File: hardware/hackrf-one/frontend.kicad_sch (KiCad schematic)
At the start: 143 parts

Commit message: HackRF One: update trace widths for new stack-up
correct or ignore ERC/DRC errors
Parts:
- C1, C11, C24, C29, C3, C33, C34, C35, C36, C37, C38, C39, C40, C45, C47, C5, C55, C57, C60, C63, C65, C66, C67, C7: value (none) -> 33pF; footprint (none) -> hackrf:GSG-0402
- C10, C16, C162, C163, C19, C2, C22, C30, C4, C54, C56, C6: value (none) -> 10nF; footprint (none) -> hackrf:GSG-0402
- C12, C13: value (none) -> 330pF; footprint (none) -> hackrf:GSG-0402
- C14: value (none) -> 8p2; footprint (none) -> hackrf:GSG-0402
- C15: value (none) -> 180pF; footprint (none) -> hackrf:GSG-0402
- C160, C41, C42, C52, C70: value (none) -> 100pF; footprint (none) -> hackrf:GSG-0402
- C161, C171, C53: value (none) -> 1uF; footprint (none) -> hackrf:GSG-0402
- C166, C17, C18, C20, C23, C25, C28, C31, C44, C46, C49, C50, C58, C59, C61, C62, C64, C9: value (none) -> 100nF; footprint (none) -> hackrf:GSG-0402
- C21, C32, C43, C48, C51, C8: value (none) -> 22pF; footprint (none) -> hackrf:GSG-0402
- C26, C27: value (none) -> 47pF; footprint (none) -> hackrf:GSG-0402
- D1: value (none) -> GSG-DIODE-TVS-BI; footprint (none) -> hackrf:GSG-0402
- J10: value (none) -> GND_CLIP; footprint (none) -> hackrf:GSG-TEST-POINT-S1751-46R
- J2: value (none) -> RF-SHIELD-FRAME; footprint (none) -> hackrf:GSG-SHIELD-BMI-S-230
- J3: value (none) -> RF-SHIELD-COVER; footprint (none) -> hackrf:GSG-NULL-MODULE
- J4, J5, J6, J7, J8, J9: value (none) -> MOUNTING_HOLE; footprint (none) -> hackrf:GSG-HOLE126MIL-COPPER
- L1, L4: value (none) -> DNP; footprint (none) -> hackrf:GSG-0402
- L12, L13, L2, L3, L5: value (none) -> 10uH; footprint (none) -> hackrf:GSG-0603
- P13: value (none) -> GPO1; footprint (none) -> hackrf:GSG-TESTPOINT-50MIL
- P17: value (none) -> GPO6; footprint (none) -> hackrf:GSG-TESTPOINT-50MIL
- P19: value (none) -> GPO3; footprint (none) -> hackrf:GSG-TESTPOINT-50MIL
- P21: value (none) -> REF_IN; footprint (none) -> hackrf:GSG-TESTPOINT-50MIL
- P27: value (none) -> MIXER_SDATA; footprint (none) -> hackrf:GSG-TESTPOINT-50MIL
- P31: value (none) -> MIXER_SCLK; footprint (none) -> hackrf:GSG-TESTPOINT-50MIL
- P32: value (none) -> MIXER_ENX; footprint (none) -> hackrf:GSG-TESTPOINT-50MIL
- P33: value (none) -> MIXER_RESETX; footprint (none) -> hackrf:GSG-TESTPOINT-50MIL
- P34: value (none) -> MIX_BYPASS; footprint (none) -> hackrf:GSG-TESTPOINT-50MIL
- P35: value (none) -> !MIX_BYPASS; footprint (none) -> hackrf:GSG-TESTPOINT-50MIL
- P4: value (none) -> ANTENNA; footprint (none) -> hackrf:GSG-SMA-73251-2120
- P43: value (none) -> RX; footprint (none) -> hackrf:GSG-TESTPOINT-50MIL
- P44: value (none) -> HP; footprint (none) -> hackrf:GSG-TESTPOINT-50MIL
- P45: value (none) -> LP; footprint (none) -> hackrf:GSG-TESTPOINT-50MIL
- P46: value (none) -> TX_MIX_BP; footprint (none) -> hackrf:GSG-TESTPOINT-50MIL
- P47: value (none) -> RX_MIX_BP; footprint (none) -> hackrf:GSG-TESTPOINT-50MIL
- P48: value (none) -> TX_AMP; footprint (none) -> hackrf:GSG-TESTPOINT-50MIL
- P49: value (none) -> RX_AMP; footprint (none) -> hackrf:GSG-TESTPOINT-50MIL
- P50: value (none) -> AMP_BYPASS; footprint (none) -> hackrf:GSG-TESTPOINT-50MIL
- P51: value (none) -> !TX_AMP_PWR; footprint (none) -> hackrf:GSG-TESTPOINT-50MIL
- P52: value (none) -> !RX_AMP_PWR; footprint (none) -> hackrf:GSG-TESTPOINT-50MIL
- P6: value (none) -> GPO4; footprint (none) -> hackrf:GSG-TESTPOINT-50MIL
- P7: value (none) -> GPO2; footprint (none) -> hackrf:GSG-TESTPOINT-50MIL
- Q1, Q2, Q4: value (none) -> MOSFET_P; footprint (none) -> gsg-modules:SOT23-3
- R1, R2: value (none) -> 470; footprint (none) -> hackrf:GSG-0402
- R24, R29, R36, R5, R6: value (none) -> 10k; footprint (none) -> hackrf:GSG-0402
- R3: value (none) -> 22k; footprint (none) -> hackrf:GSG-0402
- R4: value (none) -> 51k; footprint (none) -> hackrf:GSG-0402
- T1: value (none) -> MIX_IN_BALUN; footprint (none) -> hackrf:GSG-B0310J50100AHF
- T2: value (none) -> MIX_OUT_BALUN; footprint (none) -> hackrf:GSG-B0310J50100AHF
- U1, U10, U11, U2, U5, U6, U7: value (none) -> SKY13453; footprint (none) -> gsg-modules:SKY13350-385LF
- U12, U14, U9: value (none) -> SKY13317; footprint (none) -> hackrf:GSG-SKY13317-373LF
- U13, U25: value (none) -> MGA-81563; footprint (none) -> hackrf:GSG-SOT363
- U3: value (none) -> RX_LOWPASS_FILTER; footprint (none) -> hackrf:GSG-LP0603
- U4: value (none) -> RFFC5072; footprint (none) -> hackrf:GSG-QFN32
- U8: value (none) -> RX_HIGHPASS_FILTER; footprint (none) -> hackrf:GSG-HP-DEA

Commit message: HackRF One: update dates
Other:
- company: Copyright 2012-2020 Great Scott Gadgets -> Copyright 2012-2022 Great Scott Gadgets
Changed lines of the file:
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@@
   (title_block
     (title "HackRF One")
-    (date "2021-09-28")
+    (date "2022-08-28")
     (rev "r9")
-    (company "Copyright 2012-2020 Great Scott Gadgets")
+    (company "Copyright 2012-2022 Great Scott Gadgets")
     (comment 1 "Michael Ossmann")
     (comment 2 "Licensed under the CERN-OHL-P v2")

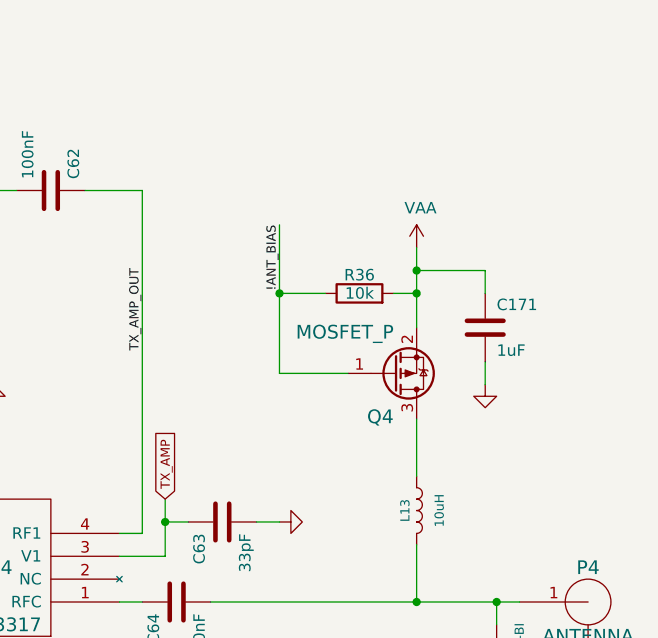
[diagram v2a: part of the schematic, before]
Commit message: HackRF One: add diode to Q4 output
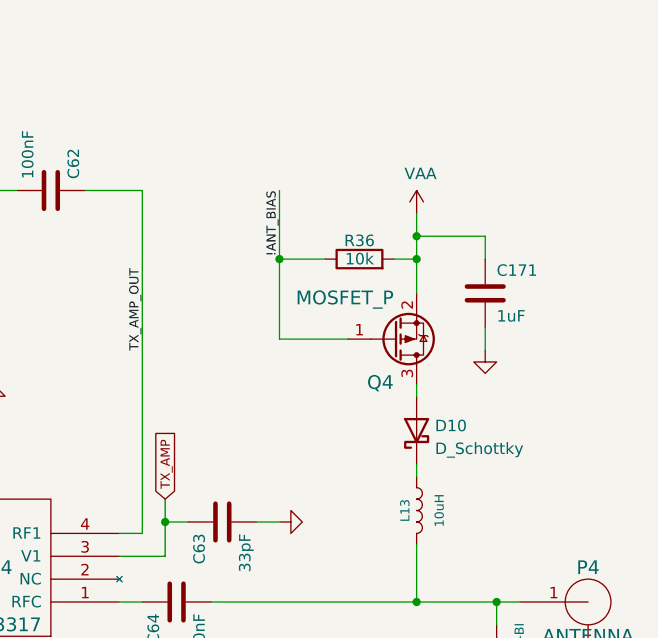
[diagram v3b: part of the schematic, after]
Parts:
- added D10: D_Schottky, gsg-modules:DSN1006-2, symbol Device:D_Schottky
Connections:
- net at L13.1: now also D10.1 (K); no longer Q4.3 (D)
- new net: D10.2 (A), Q4.3 (D)
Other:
- moved on the sheet: C171, Q4, R36

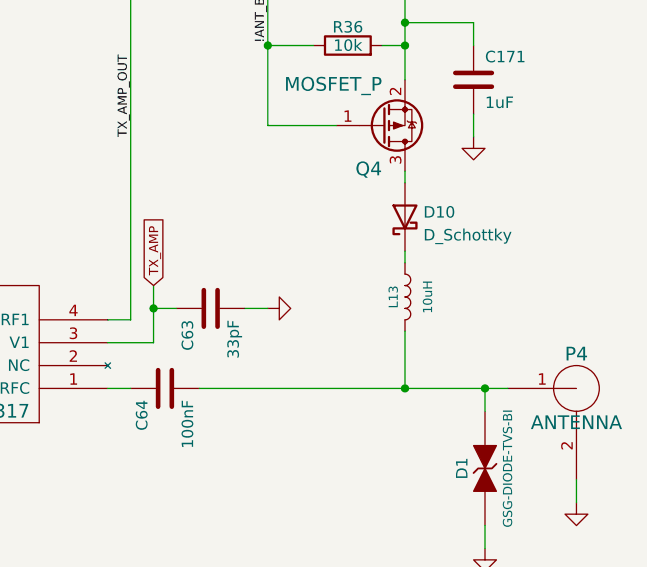
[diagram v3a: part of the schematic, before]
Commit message: HackRF One: add diode bypass jumper
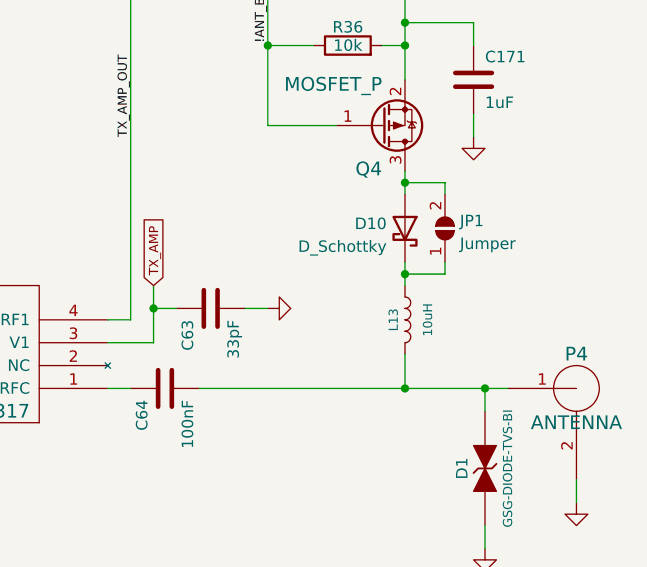
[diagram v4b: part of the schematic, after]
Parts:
- added JP1: Jumper, gsg-modules:0603-JUMPER, symbol Jumper:SolderJumper_2_Open
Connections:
- net at D10.1 (K), L13.1: now also JP1.1 (A)
- net at D10.2 (A), Q4.3 (D): now also JP1.2 (B)
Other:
- moved on the sheet: D10, L13
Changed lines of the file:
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@@
   (junction (at 160.02 212.09) (diameter 0) (color 0 0 0 0)
   )
+  (junction (at 394.97 191.77) (diameter 0) (color 0 0 0 0)
+  )
   (junction (at 379.73 176.53) (diameter 0) (color 0 0 0 0)
   )
@@
   (junction (at 146.05 204.47) (diameter 0) (color 0 0 0 0)
   )
+  (junction (at 394.97 201.93) (diameter 0) (color 0 0 0 0)
+  )
   (junction (at 297.18 168.91) (diameter 0) (color 0 0 0 0)
   )
@@
     (stroke (width 0) (type default) (color 0 0 0 0))
   )
+  (wire (pts (xy 394.97 191.77) (xy 394.97 193.04))
+    (stroke (width 0) (type default) (color 0 0 0 0))
+  )
   (wire (pts (xy 364.49 207.01) (xy 361.95 207.01))
     (stroke (width 0) (type default) (color 0 0 0 0))
@@
     (stroke (width 0) (type default) (color 0 0 0 0))
   )
-  (wire (pts (xy 394.97 199.39) (xy 394.97 200.66))
+  (wire (pts (xy 394.97 200.66) (xy 394.97 201.93))
     (stroke (width 0) (type default) (color 0 0 0 0))
   )
@@
     (stroke (width 0) (type default) (color 0 0 0 0))
   )
+  (wire (pts (xy 394.97 191.77) (xy 399.415 191.77))
+    (stroke (width 0) (type default) (color 0 0 0 0))
+  )
   (wire (pts (xy 171.45 147.32) (xy 171.45 149.86))
     (stroke (width 0) (type default) (color 0 0 0 0))
@@
     (stroke (width 0) (type default) (color 0 0 0 0))
   )
+  (wire (pts (xy 399.415 201.93) (xy 399.415 200.66))
+    (stroke (width 0) (type default) (color 0 0 0 0))
+  )
   (wire (pts (xy 129.54 110.49) (xy 129.54 107.95))
     (stroke (width 0) (type default) (color 0 0 0 0))
   )
+  (wire (pts (xy 394.97 201.93) (xy 394.97 203.2))
+    (stroke (width 0) (type default) (color 0 0 0 0))
+  )
   (wire (pts (xy 146.05 212.09) (xy 153.67 212.09))
     (stroke (width 0) (type default) (color 0 0 0 0))
@@
     (stroke (width 0) (type default) (color 0 0 0 0))
   )
-  (wire (pts (xy 394.97 208.28) (xy 394.97 214.63))
+  (wire (pts (xy 394.97 210.82) (xy 394.97 214.63))
     (stroke (width 0) (type default) (color 0 0 0 0))
   )
@@
     (stroke (width 0) (type default) (color 0 0 0 0))
   )
+  (wire (pts (xy 394.97 201.93) (xy 399.415 201.93))
+    (stroke (width 0) (type default) (color 0 0 0 0))
+  )
   (wire (pts (xy 340.36 140.97) (xy 340.36 143.51))
     (stroke (width 0) (type default) (color 0 0 0 0))
@@
     (stroke (width 0) (type default) (color 0 0 0 0))
   )
+  (wire (pts (xy 399.415 191.77) (xy 399.415 193.04))
+    (stroke (width 0) (type default) (color 0 0 0 0))
+  )
   (wire (pts (xy 232.41 205.74) (xy 232.41 203.2))
     (stroke (width 0) (type default) (color 0 0 0 0))
@@
     (pin "2")
   )
-  (symbol (lib_id "Device:L") (at 394.97 204.47 0) (unit 1)
+  (symbol (lib_id "Device:L") (at 394.97 207.01 0) (unit 1)
     (in_bom yes) (on_board yes)
-    (property "Reference" "L13" (id 0) (at 393.7 204.47 90)
+    (property "Reference" "L13" (id 0) (at 393.7 207.01 90)
       (effects (font (size 1.016 1.016)))
     )
-    (property "Value" "10uH" (id 1) (at 397.51 204.47 90)
+    (property "Value" "10uH" (id 1) (at 397.51 207.01 90)
       (effects (font (size 1.016 1.016)))
     )
-    (property "Footprint" "hackrf:GSG-0603" (id 2) (at 394.97 204.47 0)
+    (property "Footprint" "hackrf:GSG-0603" (id 2) (at 394.97 207.01 0)
       (effects (font (size 1.524 1.524)) hide)
     )
-    (property "Datasheet" "" (id 3) (at 394.97 204.47 0)
+    (property "Datasheet" "" (id 3) (at 394.97 207.01 0)
       (effects (font (size 1.524 1.524)) hide)
     )
-    (property "Manufacturer" "Taiyo Yuden" (id 4) (at 394.97 204.47 0)
+    (property "Manufacturer" "Taiyo Yuden" (id 4) (at 394.97 207.01 0)
       (effects (font (size 1.524 1.524)) hide)
     )
-    (property "Part Number" "BRL1608T100M" (id 5) (at 394.97 204.47 0)
+    (property "Part Number" "BRL1608T100M" (id 5) (at 394.97 207.01 0)
       (effects (font (size 1.524 1.524)) hide)
     )
-    (property "Description" "INDUCTR 10UH 220MA 20% 0603 SMD" (id 6) (at 394.97 204.47 0)
+    (property "Description" "INDUCTR 10UH 220MA 20% 0603 SMD" (id 6) (at 394.97 207.01 0)
       (effects (font (size 1.524 1.524)) hide)
     )
@@
     (pin "1")
   )
-  (symbol (lib_id "Device:D_Schottky") (at 394.97 195.58 90) (unit 1)
-    (in_bom yes) (on_board yes) (fields_autoplaced)
-    (property "Reference" "D10" (id 0) (at 397.002 195.0628 90)
+  (symbol (lib_id "Device:D_Schottky") (at 394.97 196.85 270) (mirror x) (unit 1)
+    (in_bom yes) (on_board yes)
+    (property "Reference" "D10" (id 0) (at 392.938 196.3328 90)
       (effects (font (size 1.27 1.27)) (justify right))
     )
-    (property "Value" "D_Schottky" (id 1) (at 397.002 197.5997 90)
+    (property "Value" "D_Schottky" (id 1) (at 392.938 198.8697 90)
       (effects (font (size 1.27 1.27)) (justify right))
     )
-    (property "Footprint" "gsg-modules:DSN1006-2" (id 2) (at 394.97 195.58 0)
+    (property "Footprint" "gsg-modules:DSN1006-2" (id 2) (at 394.97 196.85 0)
+      (effects (font (size 1.27 1.27)) hide)
+    )
+    (property "Datasheet" "~" (id 3) (at 394.97 196.85 0)
       (effects (font (size 1.27 1.27)) hide)
     )
-    (property "Datasheet" "~" (id 3) (at 394.97 195.58 0)
+    (property "Description" "DIODE SCHOTTKY 40V 1A DSN1006-2" (id 4) (at 394.97 196.85 0)
       (effects (font (size 1.27 1.27)) hide)
     )
-    (property "Description" "DIODE SCHOTTKY 40V 1A DSN1006-2" (id 4) (at 394.97 195.58 0)
+    (property "Manufacturer" "Nexperia" (id 5) (at 394.97 196.85 0)
       (effects (font (size 1.27 1.27)) hide)
     )
-    (property "Manufacturer" "Nexperia" (id 5) (at 394.97 195.58 0)
+    (property "Part Number" "PMEG4010ESBYL" (id 6) (at 394.97 196.85 0)
+      (effects (font (size 1.27 1.27)) hide)
+    )
+    (pin "1")
+    (pin "2")
+  )
+  (symbol (lib_id "Jumper:SolderJumper_2_Open") (at 399.415 196.85 90) (unit 1)
+    (in_bom yes) (on_board yes) (fields_autoplaced)
+    (property "Reference" "JP1" (id 0) (at 401.066 196.0153 90)
+      (effects (font (size 1.27 1.27)) (justify right))
+    )
+    (property "Value" "Jumper" (id 1) (at 401.066 198.5522 90)
+      (effects (font (size 1.27 1.27)) (justify right))
+    )
+    (property "Footprint" "gsg-modules:0603-JUMPER" (id 2) (at 399.415 196.85 0)
       (effects (font (size 1.27 1.27)) hide)
     )
-    (property "Part Number" "PMEG4010ESBYL" (id 6) (at 394.97 195.58 0)
+    (property "Datasheet" "~" (id 3) (at 399.415 196.85 0)
       (effects (font (size 1.27 1.27)) hide)
     )

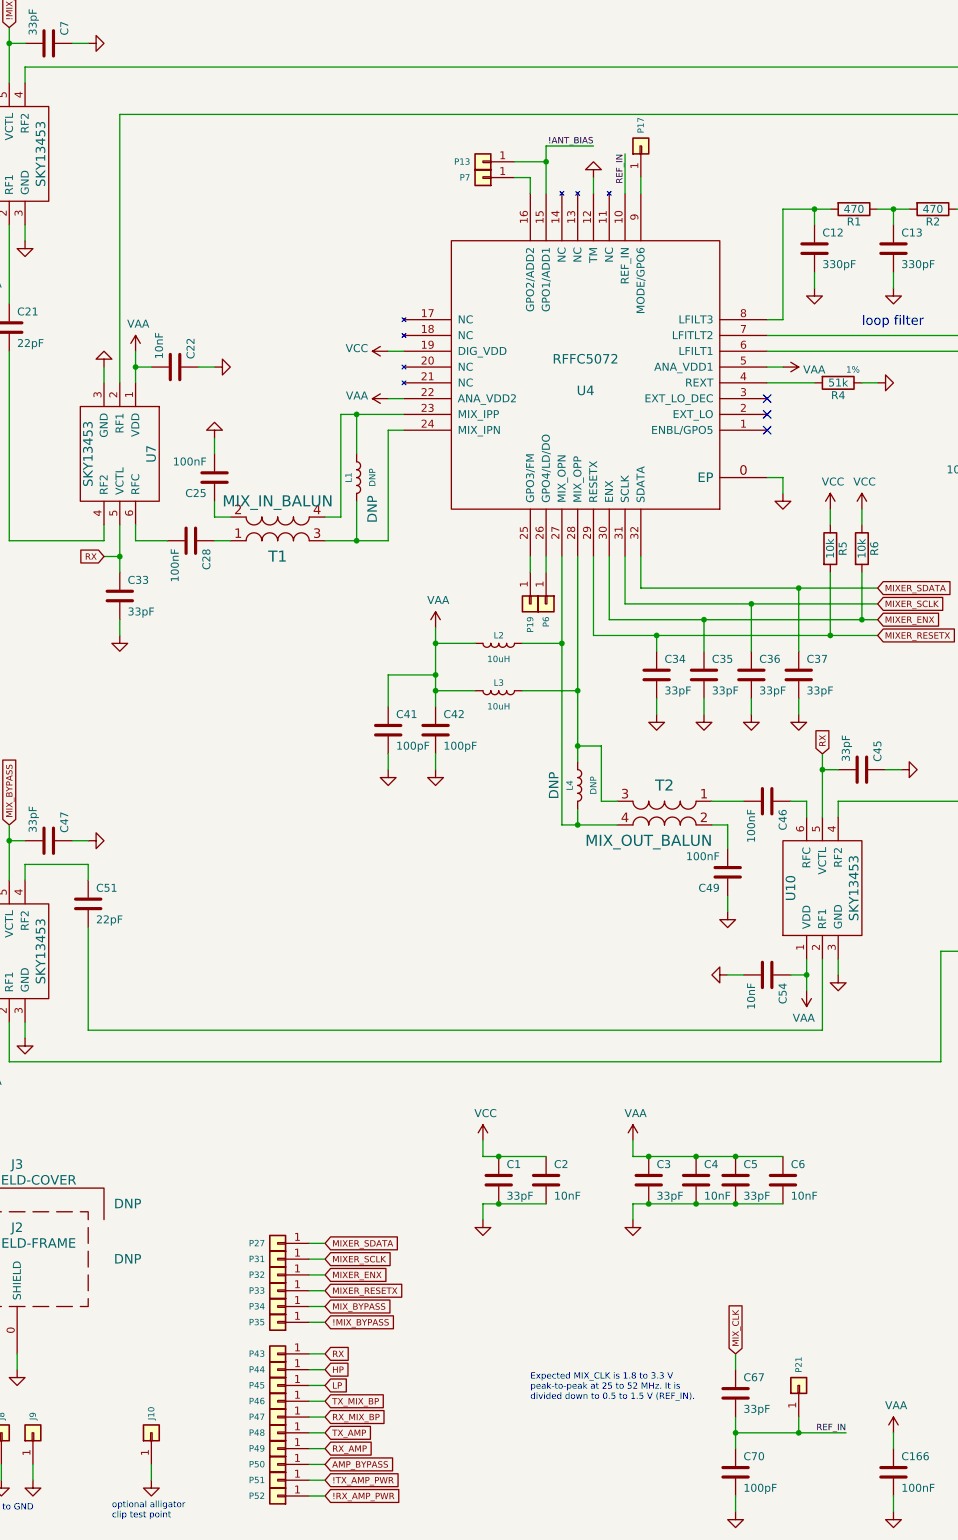
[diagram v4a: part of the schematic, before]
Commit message: HackRF One: change U19 from Si5351C to Si5351A
add clock distribution and detection
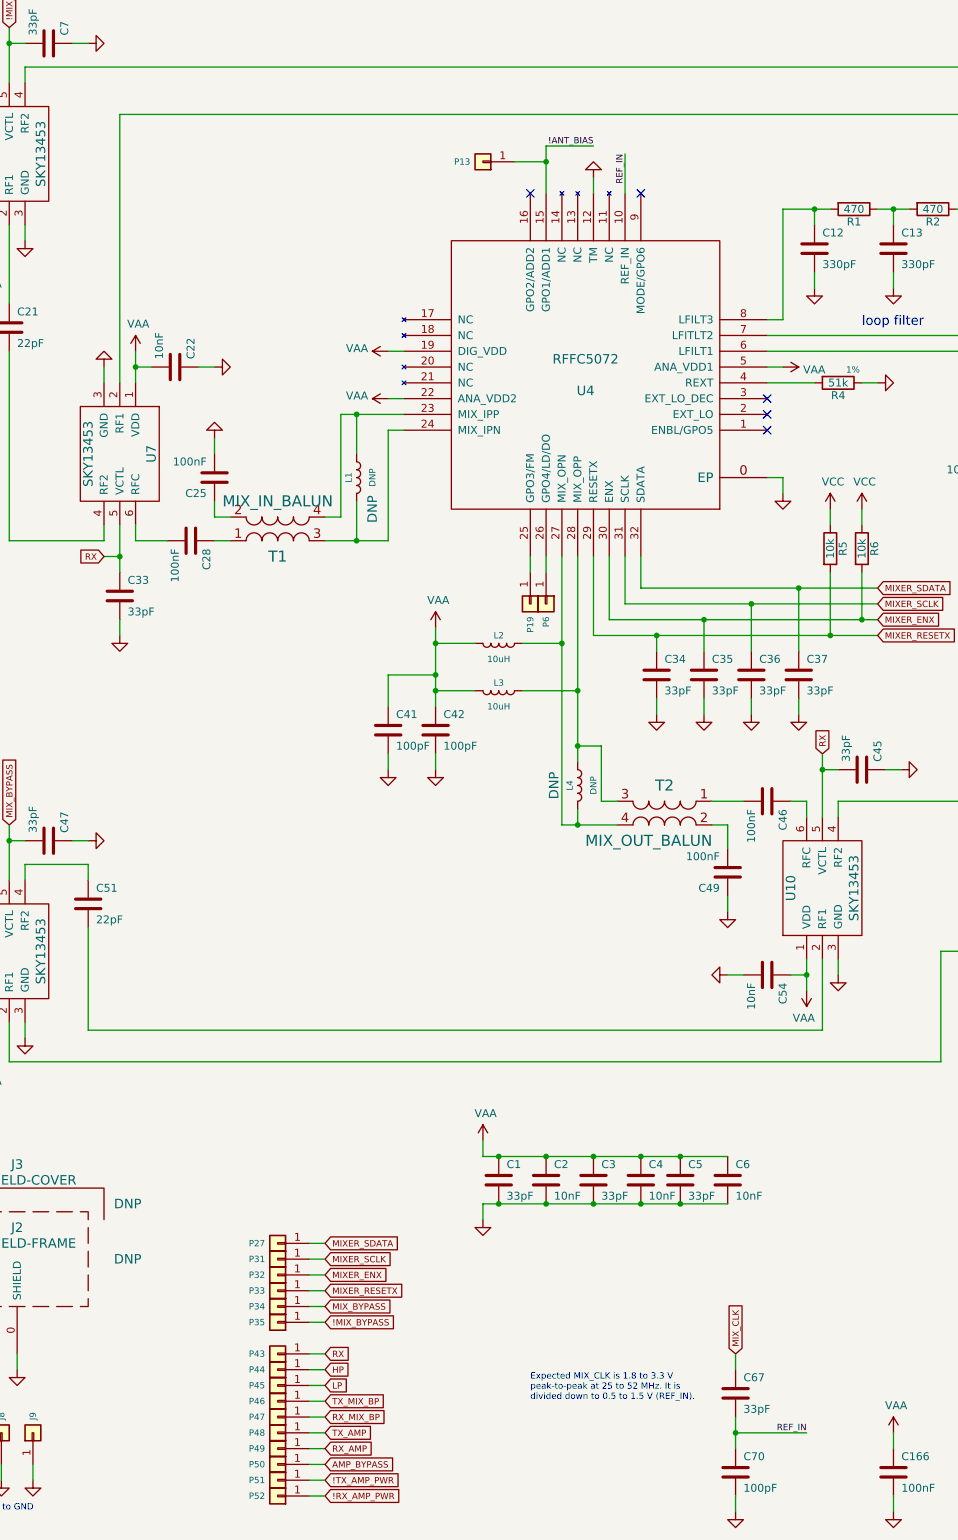
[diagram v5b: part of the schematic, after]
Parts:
- removed J10: GND_CLIP, hackrf:GSG-TEST-POINT-S1751-46R, symbol Connector_Generic:Conn_01x01
- removed P17: GPO6, hackrf:GSG-TESTPOINT-50MIL, symbol Connector_Generic:Conn_01x01
- removed P21: REF_IN, hackrf:GSG-TESTPOINT-50MIL, symbol Connector_Generic:Conn_01x01
- removed P7: GPO2, hackrf:GSG-TESTPOINT-50MIL, symbol Connector_Generic:Conn_01x01
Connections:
- net VAA: now also C1.1, C2.1, U4.19 (DIG_VDD)
- net VCC: no longer C1.1, C2.1, U4.19 (DIG_VDD)
- no-connect marks 3 -> 5
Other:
- note removed: "optional alligator clip test point"
- moved on the sheet: C3, C4, C5, C6
